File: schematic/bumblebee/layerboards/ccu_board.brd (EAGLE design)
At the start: 85 x 35 mm, 14 parts

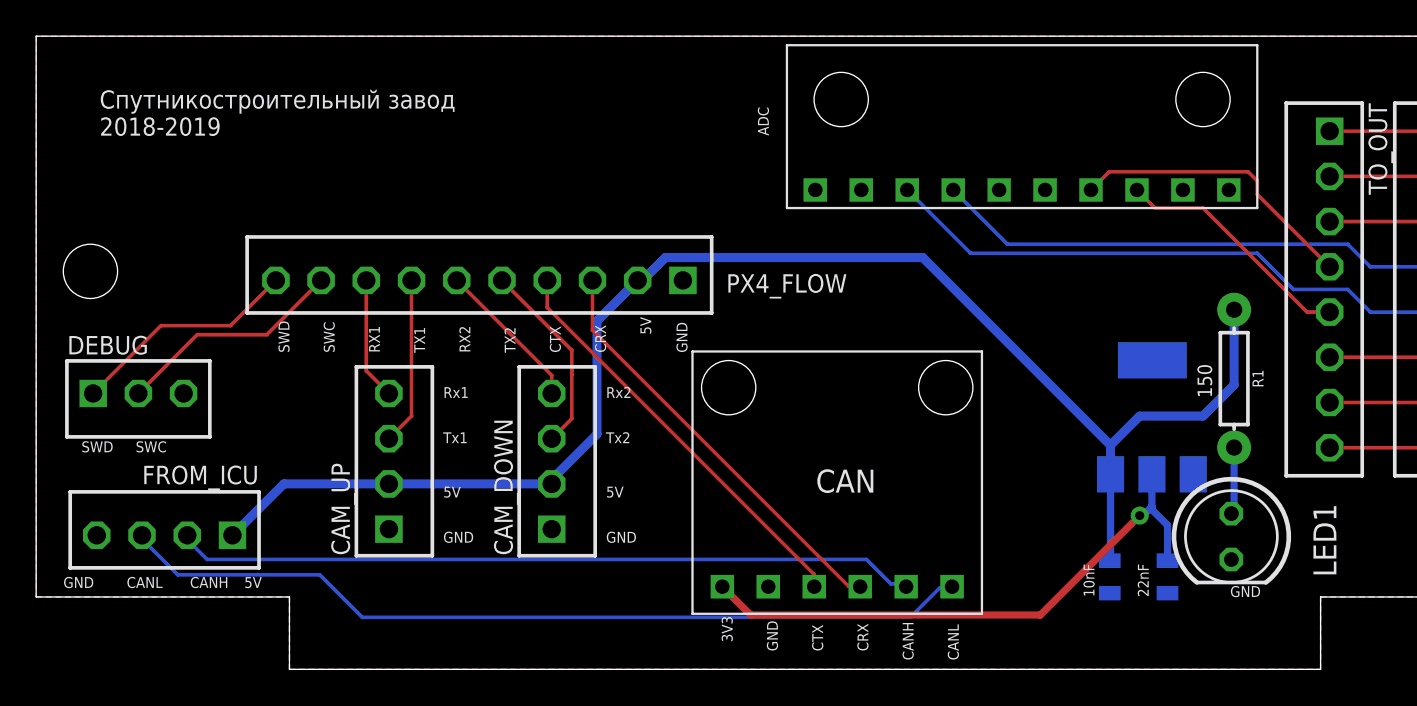
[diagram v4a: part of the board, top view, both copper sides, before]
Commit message: Исправил библиотеку Осталось исправить внешнюю плату и сделать плату под антенну GPS
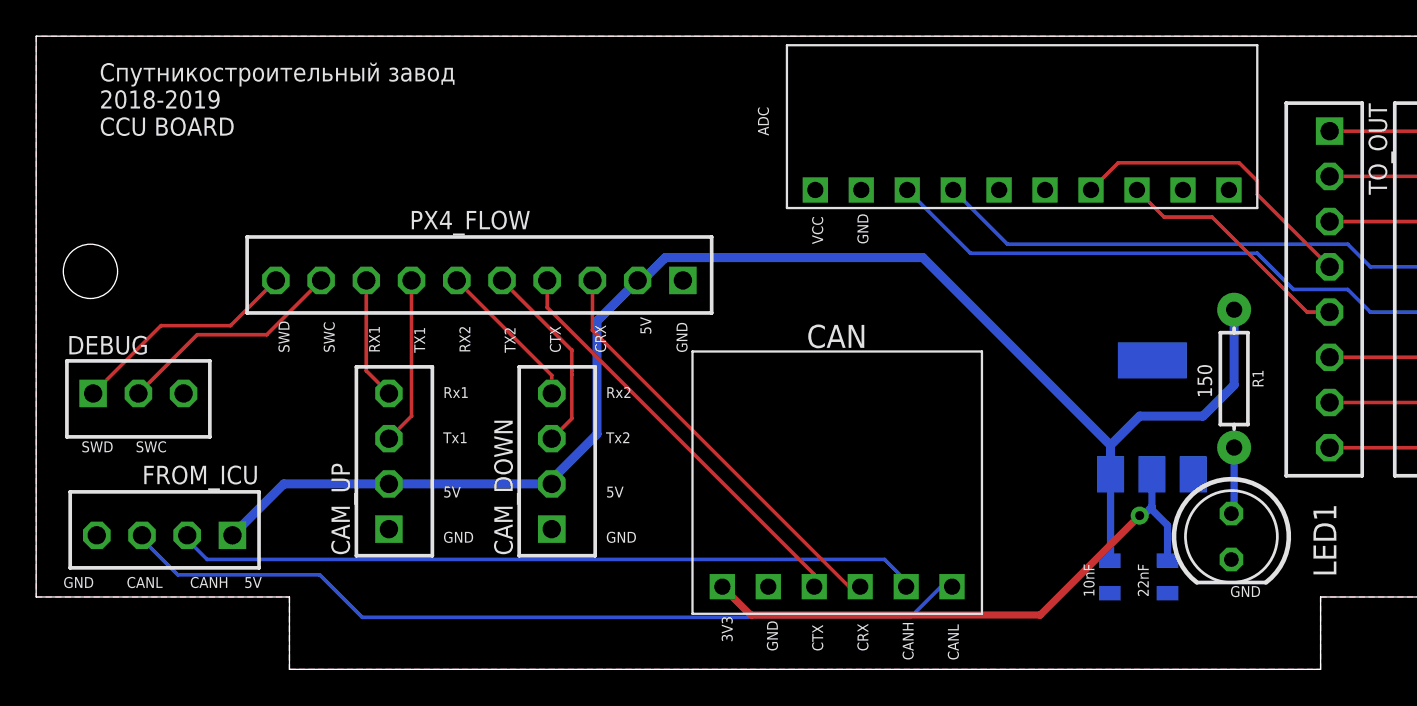
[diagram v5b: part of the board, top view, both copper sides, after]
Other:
- board text added: "VCC"
- board text added: "Спутникостроительный завод 2018-2019 CCU BOARD"
- board text removed: "Спутникостроительный завод 2018-2019"
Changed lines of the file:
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@@
 <layer number="115" name="ReferenceISLANDS" color="7" fill="1" visible="no" active="no"/>
 <layer number="116" name="Patch_BOT" color="9" fill="4" visible="no" active="no"/>
+<layer number="117" name="BACKMAAT1" color="7" fill="1" visible="yes" active="yes"/>
 <layer number="118" name="Rect_Pads" color="7" fill="1" visible="no" active="no"/>
+<layer number="119" name="KAP_TEKEN" color="7" fill="1" visible="yes" active="yes"/>
+<layer number="120" name="KAP_MAAT1" color="7" fill="1" visible="yes" active="yes"/>
 <layer number="121" name="_tsilk" color="7" fill="1" visible="no" active="no"/>
 <layer number="122" name="_bsilk" color="7" fill="1" visible="no" active="no"/>
@@
 <layer number="128" name="_bValues" color="7" fill="1" visible="no" active="no"/>
 <layer number="129" name="Mask" color="7" fill="1" visible="no" active="no"/>
+<layer number="130" name="SMDSTROOK" color="7" fill="1" visible="yes" active="yes"/>
 <layer number="131" name="tAdjust" color="7" fill="1" visible="no" active="no"/>
 <layer number="132" name="bAdjust" color="7" fill="1" visible="no" active="no"/>
@@
 <text x="66" y="4" size="0.6" layer="21">GND</text>
 <text x="3.5" y="29.5" size="1" layer="21">Спутникостроительный завод
-2018-2019</text>
+2018-2019
+CCU BOARD</text>
 <text x="40.5" y="29.5" size="0.6" layer="21" rot="R90">ADC</text>
+<text x="43.5" y="23.5" size="0.6" layer="21" rot="R90">VCC</text>
+<text x="46" y="23.5" size="0.6" layer="21" rot="R90">GND</text>
 </plain>
 <attributes>
@@
 </element>
 <element name="CAN" library="bluepill" package="CAN" value="CAN" x="44.28" y="10.32" smashed="yes" rot="R90">
-<attribute name="NAME" x="46.43" y="11.04" size="1.27" layer="25" rot="R180"/>
+<attribute name="NAME" x="45.93" y="19.04" size="1.27" layer="25" rot="R180"/>
 <attribute name="VALUE" x="54.9" y="3.31" size="1.27" layer="27" rot="R90"/>
 </element>
@@
 </element>
 <element name="PX4_FLOW" library="con-jst-eh" package="B10B-EH-A" value="B10B-EH-A" x="24.5" y="21.5" smashed="yes" rot="R180">
-<attribute name="NAME" x="44.827" y="21.841" size="1.016" layer="25" ratio="18" rot="R180"/>
+<attribute name="NAME" x="27.327" y="25.341" size="1.016" layer="25" ratio="18" rot="R180"/>
 <attribute name="VALUE" x="37.327" y="25.183" size="1.016" layer="27" ratio="10" rot="R180"/>
 </element>
@@
 <contactref element="CAN" pad="CANH"/>
 <contactref element="FROM_ICU" pad="2"/>
-<wire x1="47.25" y1="4.725" x2="47.925" y2="4.725" width="0.2" layer="16"/>
-<wire x1="45.9" y1="6.075" x2="47.25" y2="4.725" width="0.2" layer="16"/>
-<wire x1="9.45" y1="6.075" x2="45.9" y2="6.075" width="0.2" layer="16"/>
+<wire x1="48.09" y1="4.57" x2="48.09" y2="4.885" width="0.2" layer="16"/>
+<wire x1="48.09" y1="4.885" x2="46.9" y2="6.075" width="0.2" layer="16"/>
+<wire x1="9.45" y1="6.075" x2="46.9" y2="6.075" width="0.2" layer="16"/>
 <wire x1="8.325" y1="7.2" x2="9.45" y2="6.075" width="0.2" layer="16"/>
-<wire x1="47.925" y1="4.725" x2="48.09" y2="4.57" width="0.2" layer="16"/>
 <wire x1="8.325" y1="7.2" x2="8.35" y2="7.41" width="0.2" layer="16"/>
 </signal>
@@
 <contactref element="U$1" pad="A1"/>
 <wire x1="71.5" y1="19.75" x2="70.25" y2="19.75" width="0.2" layer="1"/>
-<wire x1="61.85" y1="25.5" x2="60.85" y2="26.5" width="0.2" layer="1"/>
-<wire x1="70.25" y1="19.75" x2="64.5" y2="25.5" width="0.2" layer="1"/>
-<wire x1="64.5" y1="25.5" x2="61.85" y2="25.5" width="0.2" layer="1"/>
+<wire x1="62.35" y1="25" x2="60.85" y2="26.5" width="0.2" layer="1"/>
+<wire x1="70.25" y1="19.75" x2="65" y2="25" width="0.2" layer="1"/>
+<wire x1="65" y1="25" x2="62.35" y2="25" width="0.2" layer="1"/>
 </signal>
 <signal name="N$13">
@@
 <wire x1="71.5" y1="22.25" x2="67.5" y2="26.25" width="0.2" layer="1"/>
 <wire x1="67.5" y1="26.25" x2="67.5" y2="27" width="0.2" layer="1"/>
-<wire x1="67.5" y1="27" x2="67" y2="27.5" width="0.2" layer="1"/>
-<wire x1="59.31" y1="27.5" x2="58.31" y2="26.5" width="0.2" layer="1"/>
-<wire x1="67" y1="27.5" x2="59.31" y2="27.5" width="0.2" layer="1"/>
+<wire x1="67.5" y1="27" x2="66.5" y2="28" width="0.2" layer="1"/>
+<wire x1="59.81" y1="28" x2="58.31" y2="26.5" width="0.2" layer="1"/>
+<wire x1="66.5" y1="28" x2="59.81" y2="28" width="0.2" layer="1"/>
 </signal>
 </signals>
